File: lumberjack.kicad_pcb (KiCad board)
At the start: 2 copper layers, 284.7 x 94.2 mm, 159 parts, among them J1 USB, J2 AVR_ISP_6, J3 JST, J4 JST, SW1 RESET, SW2 BOOT, U1 ATMEGA328-PU, Y1 16MHz

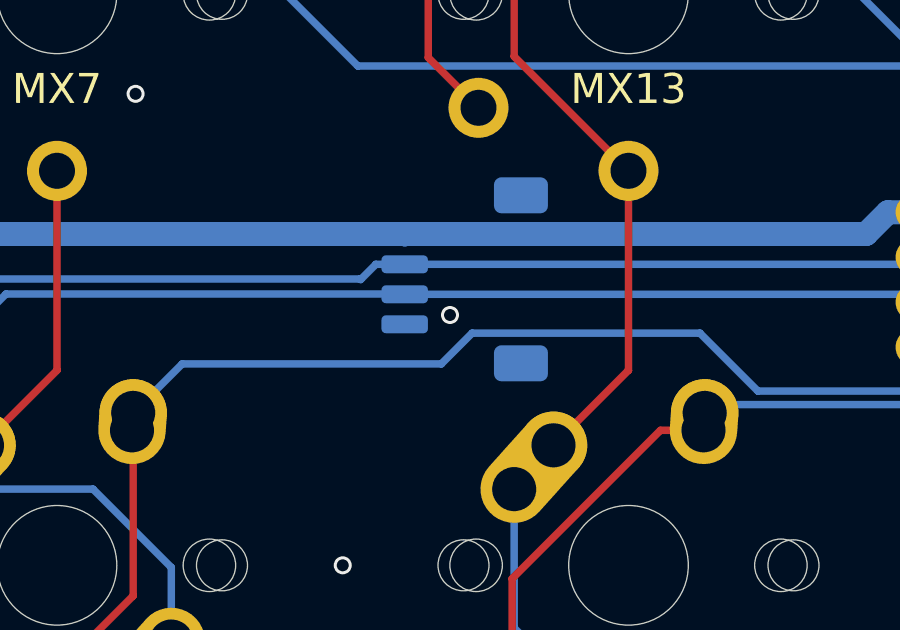
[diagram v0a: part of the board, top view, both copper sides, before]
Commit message: Revert to more spacious hybrid USB design
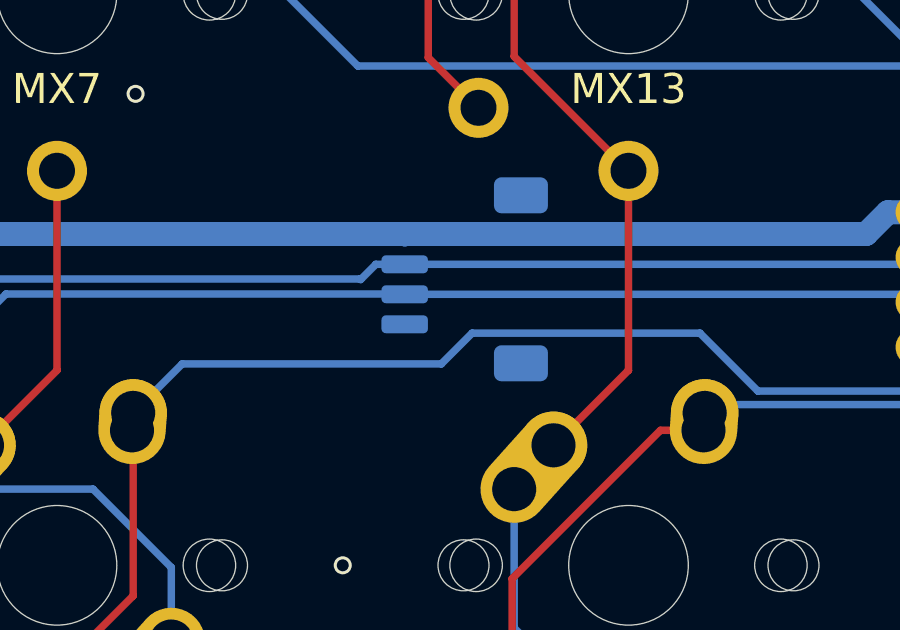
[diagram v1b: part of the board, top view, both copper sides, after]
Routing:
- net GND: vias 16 -> 15

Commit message: Add extra standoff mounting holes
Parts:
- added H10: M2, lumberjack:MountingHole_M2, F.Cu at (276.2, 73.8)
- added H11: M2, lumberjack:MountingHole_M2, F.Cu at (276.2, 131.0)
- added H8: M2, lumberjack:MountingHole_M2, F.Cu at (28.6, 73.8)
- added H9: M2, lumberjack:MountingHole_M2, F.Cu at (28.6, 131.0)
- moved R6 16.9 mm to (41.7, 73.8), turned to 180 degrees
- moved R5 16.9 mm to (15.5, 73.8), turned to 0 degrees
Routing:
- net GND: track 11.3 -> 31.2 mm, vias 15 -> 16
- net /COL1: track 284.6 -> 278.5 mm
- net Net-(F1-Pad1): track 212.6 -> 215.2 mm
- net Net-(D32-Pad2): track 130.2 -> 128.1 mm
- net Net-(J1-PadCC1): track 18.1 -> 16.3 mm
- net Net-(D1-Pad2): track 149.2 -> 148.3 mm
- net Net-(J1-PadCC2): track 24.2 -> 24.7 mm

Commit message: Bump rev number on silkscreen
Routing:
- net Net-(F1-Pad1): track 215.2 -> 214.6 mm
- net GND: vias 16 -> 17
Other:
- board text added: "rev1.6 02/2022"
- board text removed: "rev1.5 12/2021"
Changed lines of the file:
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@@
     (thickness 1.6)
     (drawings 174)
-    (tracks 1301)
+    (tracks 1302)
     (zones 0)
     (modules 163)
@@
     (arrow2b (pts (xy 9.884735 36.344325) (xy 11.010753 35.756973)))
   )
-  (gr_text "rev1.5\n12/2021" (at 233.35 93.2) (layer B.Mask)
+  (gr_text "rev1.6\n02/2022" (at 233.35 93.2) (layer B.Mask)
     (effects (font (size 1 1) (thickness 0.2)) (justify left mirror))
   )
@@
   (segment (start 68.931244 76.075) (end 69.056308 76.200064) (width 0.25) (layer B.Cu) (net 2))
   (segment (start 68.586059 76.075) (end 68.931244 76.075) (width 0.25) (layer B.Cu) (net 2))
+  (via (at 25.003146 68.460995) (size 0.6) (drill 0.4) (layers F.Cu B.Cu) (net 2))
   (segment (start 167.362311 76.795377) (end 168.473579 76.795377) (width 0.25) (layer B.Cu) (net 3) (status 20))
   (segment (start 162.40138 81.756308) (end 167.362311 76.795377) (width 0.25) (layer B.Cu) (net 3) (status 10))
@@
   (segment (start 49.69 72.311894) (end 49.701894 72.3) (width 0.8) (layer B.Cu) (net 24) (status 30))
   (segment (start 49.69 72.31) (end 49.69 72.311894) (width 0.8) (layer B.Cu) (net 24) (status 30))
-  (segment (start 49.39 72.01) (end 49.69 72.31) (width 0.8) (layer B.Cu) (net 24))
-  (segment (start 31.528716 72.01) (end 49.39 72.01) (width 0.8) (layer B.Cu) (net 24))
-  (segment (start 29.76565 70.246934) (end 31.528716 72.01) (width 0.8) (layer B.Cu) (net 24))
-  (segment (start 25.598459 70.246934) (end 29.76565 70.246934) (width 0.8) (layer B.Cu) (net 24))
-  (segment (start 25.999969 69.845424) (end 25.999969 64.110031) (width 0.8) (layer B.Cu) (net 24))
+  (segment (start 26.5 69.345393) (end 26.5 63.61) (width 0.8) (layer B.Cu) (net 24))
   (segment (start 25.003146 76.200064) (end 25.003146 70.842247) (width 0.8) (layer B.Cu) (net 24))
-  (segment (start 25.999969 64.110031) (end 26.5 63.61) (width 0.8) (layer B.Cu) (net 24))
-  (segment (start 26.789085 106.561027) (end 26.789085 77.986003) (width 0.8) (layer B.Cu) (net 24))
-  (segment (start 32.403003 112.174945) (end 26.789085 106.561027) (width 0.8) (layer B.Cu) (net 24))
-  (segment (start 25.003146 70.842247) (end 25.999969 69.845424) (width 0.8) (layer B.Cu) (net 24))
-  (segment (start 140.493868 113.546035) (end 140.125745 113.914158) (width 0.8) (layer B.Cu) (net 24))
-  (segment (start 120.862228 112.174945) (end 32.403003 112.174945) (width 0.8) (layer B.Cu) (net 24))
   (segment (start 26.789085 77.986003) (end 25.003146 76.200064) (width 0.8) (layer B.Cu) (net 24))
+  (segment (start 32.403003 112.174945) (end 26.789085 106.561027) (width 0.8) (layer B.Cu) (net 24))
   (segment (start 122.601441 113.914158) (end 120.862228 112.174945) (width 0.8) (layer B.Cu) (net 24))
+  (segment (start 25.003146 70.842247) (end 26.5 69.345393) (width 0.8) (layer B.Cu) (net 24))
+  (segment (start 120.862228 112.174945) (end 32.403003 112.174945) (width 0.8) (layer B.Cu) (net 24))
   (segment (start 140.125745 113.914158) (end 122.601441 113.914158) (width 0.8) (layer B.Cu) (net 24))
+  (segment (start 26.789085 106.561027) (end 26.789085 77.986003) (width 0.8) (layer B.Cu) (net 24))
+  (segment (start 140.493868 113.546035) (end 140.125745 113.914158) (width 0.8) (layer B.Cu) (net 24))
+  (segment (start 26.806228 69.651621) (end 26.5 69.345393) (width 0.8) (layer B.Cu) (net 24))
+  (segment (start 29.170337 69.651621) (end 26.806228 69.651621) (width 0.8) (layer B.Cu) (net 24))
+  (segment (start 31.528716 72.01) (end 29.170337 69.651621) (width 0.8) (layer B.Cu) (net 24))
+  (segment (start 49.39 72.01) (end 31.528716 72.01) (width 0.8) (layer B.Cu) (net 24))
+  (segment (start 49.69 72.31) (end 49.39 72.01) (width 0.8) (layer B.Cu) (net 24))
   (segment (start 21.57657 60.843594) (end 21.589968 60.830196) (width 0.25) (layer F.Cu) (net 25) (status 30))
   (segment (start 21.589968 60.830196) (end 21.589968 59.21375) (width 0.25) (layer F.Cu) (net 25) (status 30))

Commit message: Add cutouts for CK Bakeneko
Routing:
- net Net-(D62-Pad1): track 246.3 -> 231.7 mm
- net GND: track 31.2 -> 40.0 mm, vias 17 -> 19
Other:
- outline, holes or cut-outs redrawn
- board text added: "rev1.7 03/2022"
- board text removed: "rev1.6 02/2022"

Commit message: Update to KiCad 6 file format
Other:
- outline, holes or cut-outs redrawn
- net class 5v removed
- net class Default removed
